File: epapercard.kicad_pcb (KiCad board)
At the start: 2 copper layers, 43 parts, among them P1 CONN_01X06, P2 A120699CT, Q1 2N7002KW, Q2 BSS84W, Q3 AP2305, Q4 BSS84W, Q5 2N7002KW, Q6 2N7002KW, Q7 2N7002KW, SW1 SW_PUSH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

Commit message: I remembered how mirrors work
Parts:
- moved R8 79.0 mm to (28.6, 69.5), turned to 270 degrees
- moved P1 73.2 mm to (31.9, 71.0), turned to 180 degrees
- moved P2 71.4 mm to (103.0, 64.6), turned to 90 degrees
- moved R5 58.6 mm to (95.1, 52.7), turned to 180 degrees
- moved R3 56.7 mm to (96.3, 39.1)
- moved C4 56.7 mm to (96.3, 35.8)
- moved Q7 55.6 mm to (95.2, 44.7), turned to 270 degrees
- moved R4 55.0 mm to (102.2, 45.6)
- moved Q4 55.0 mm to (107.8, 45.6)
- moved Q1 53.5 mm to (40.8, 59.6), turned to 180 degrees
- moved R1 48.1 mm to (44.1, 56.3), turned to 180 degrees
- moved D2 47.2 mm to (57.4, 72.4)
- moved SW1 46.4 mm to (40.2, 73.7), turned to 180 degrees
- moved C14 44.3 mm to (47.1, 53.2), turned to 180 degrees
- moved R7 42.0 mm to (57.4, 68.6), turned to 180 degrees
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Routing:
- net BORDER_CONTROL: track 42.3 -> 109.9 mm
- net +3V3: track 154.4 -> 210.3 mm, vias 2 -> 3
- net /button: track 73.8 -> 25.3 mm
- net /led: track 46.6 -> 4.74 mm
- net GND: track 24.3 -> 61.2 mm, vias 0 -> 2
- net DISCHARGE: track 0.00 -> 26.9 mm, vias 0 -> 3
- net PWM: track 0.00 -> 25.0 mm, vias 0 -> 2
- net /VDH: track 59.9 -> 39.9 mm
- net +3.3VP: track 93.1 -> 74.4 mm, vias 2 -> 0
- net /BORDER: track 27.0 -> 17.5 mm, vias 2 -> 0
- net Net-(Q7-Pad1): track 9.79 -> 17.4 mm
- net Net-(D2-Pad2): track 0.00 -> 3.85 mm
- net SPI_CLK: track 57.6 -> 55.4 mm
- net /test: track 15.5 -> 17.0 mm
- net SPI_MOSI: track 58.9 -> 57.7 mm
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- added copper zone on B.Cu, net GND
- added copper zone on F.Cu, net GND
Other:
- board outline added: 88.9 x 50.8 mm
- net class Default: trace_width 0.1524 -> 0.254
- board text added: "CUT OUT"
- board text added: "Paul Schow"
- board text added: "paulschow.com"
- board text added: "paulschow@gmail.com"

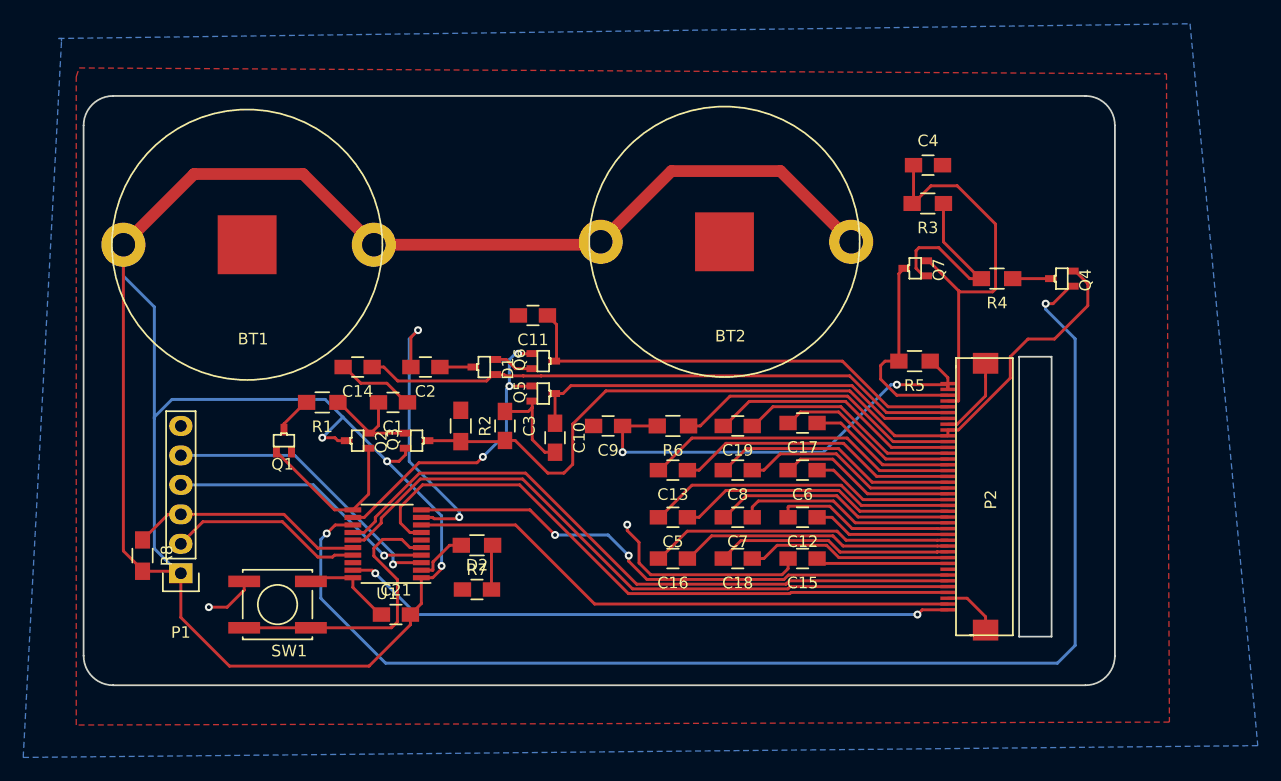
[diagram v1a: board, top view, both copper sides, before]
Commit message: Switched to surface mount battery holders
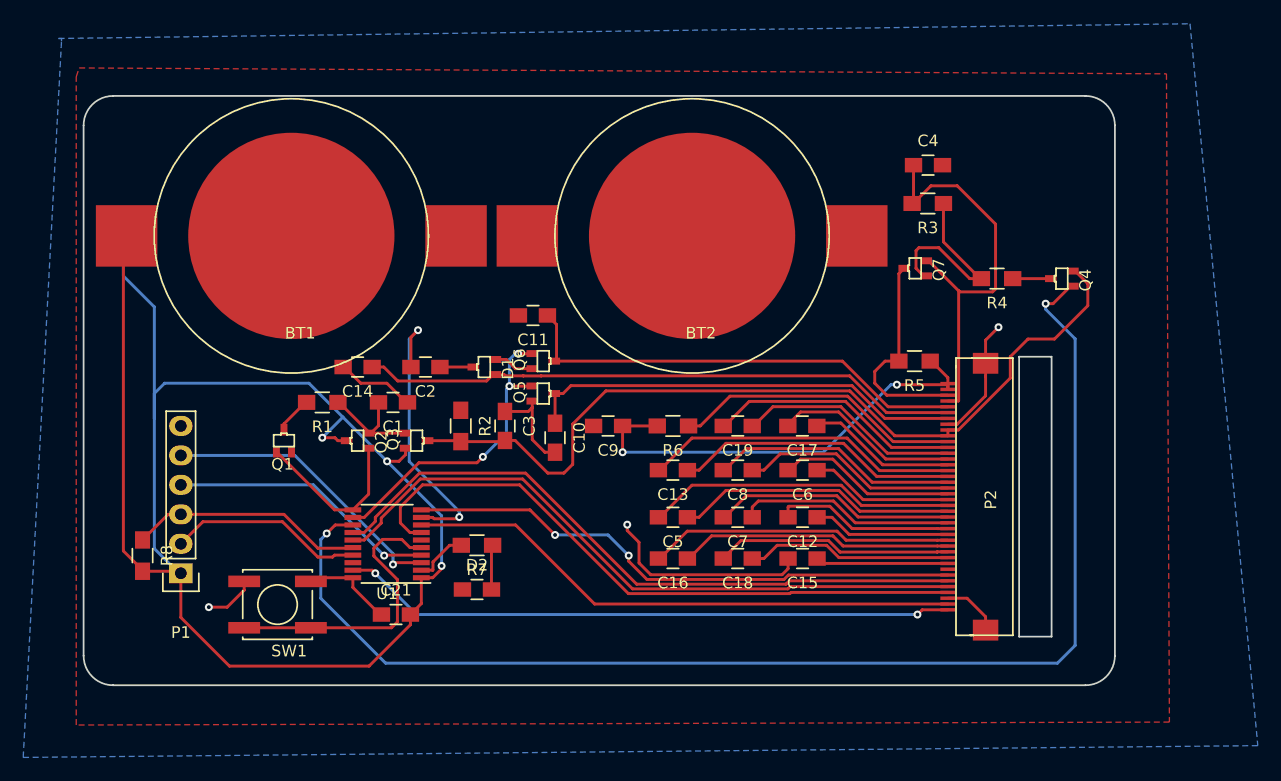
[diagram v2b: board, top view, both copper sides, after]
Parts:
- BT1, BT2: footprint footprint:CR2032 -> footprint:CR2032sm
- moved BT1 4.10 mm to (41.4, 41.9)
- moved BT2 2.55 mm to (75.9, 41.9)
- moved C17 0.25 mm to (85.5, 58.3)
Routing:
- net +3V3: track 210.3 -> 139.7 mm
- net GND: track 61.2 -> 64.8 mm, vias 2 -> 3
- net /BORDER: track 17.5 -> 18.4 mm

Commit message: Minor tweaks
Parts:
- moved C14 10.1 mm to (37.7, 57.0), turned to 270 degrees
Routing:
- net +3V3: track 139.7 -> 226.8 mm
- net /VGL: track 51.7 -> 63.4 mm
- net GND: track 64.8 -> 58.1 mm

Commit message: Connected everything
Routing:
- net +3V3: track 226.8 -> 233.9 mm, vias 3 -> 4
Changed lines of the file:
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@@
     (links 104)
     (no_connects 0)
-    (area 23.419999 29.769999 112.470001 80.720001)
+    (area 8.204287 22.759999 124.714001 86.868001)
     (thickness 1.6)
     (drawings 22)
-    (tracks 447)
+    (tracks 452)
     (zones 0)
     (modules 43)
@@
   )
   (setup
-    (last_trace_width 0.508)
+    (last_trace_width 0.254)
     (user_trace_width 0.254)
     (user_trace_width 0.381)
@@
     (pad_to_mask_clearance 0.2)
     (aux_axis_origin 0 0)
-    (visible_elements FFFFE7FF)
+    (visible_elements FFFFEFFF)
     (pcbplotparams
       (layerselection 0x010f0_80000001)
@@
     (arrow2b (pts (xy 19.05 81.28) (xy 20.176504 80.693579)))
   )
+  (segment (start 29.21 47.244) (end 27.202 45.236) (width 0.254) (layer F.Cu) (net 1))
+  (segment (start 27.202 45.236) (end 27.202 41.91) (width 0.254) (layer F.Cu) (net 1))
+  (segment (start 29.591 48.033076) (end 29.591 47.625) (width 0.254) (layer B.Cu) (net 1))
+  (segment (start 29.591 47.625) (end 29.21 47.244) (width 0.254) (layer B.Cu) (net 1))
+  (via (at 29.21 47.244) (size 0.6858) (drill 0.3302) (layers F.Cu B.Cu) (net 1))
   (segment (start 90.146 41.91) (end 90.146 37.2378) (width 1.016) (layer F.Cu) (net 1))
   (segment (start 90.146 37.2378) (end 84.1502 31.242) (width 1.016) (layer F.Cu) (net 1))
